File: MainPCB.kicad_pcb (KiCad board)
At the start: 4 copper layers, 105 x 62.4 mm, 57 parts, among them J1 RaspberryPi, J2 Conn_01x05, J3 Screw_Terminal_01x02, J4 Conn_01x02, J5 Conn_01x06, J6 Conn_01x03_Pin, J7 Conn_01x05, J8 Conn_01x12, M1 Motor_DC, M2 Motor_DC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

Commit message: moved more stuff
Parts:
- added J10: Conn_01x02, Connector_PinHeader_2.54mm:PinHeader_1x02_P2.54mm_Vertical, F.Cu at (131.6, 65.5)
- added J9: Conn_01x02, Connector_PinHeader_2.54mm:PinHeader_1x02_P2.54mm_Vertical, F.Cu at (111.8, 120.9)
- moved J2 3.65 mm to (189.5, 93.1)
- moved M1 1.79 mm to (115.1, 82.1)
- moved M4 0.93 mm to (124.5, 74.2)
- moved U5 0.63 mm to (128.3, 76.6)
- moved R1 0.51 mm to (99.6, 93.5)
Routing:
- net 12V: track 228.8 -> 0.00 mm
- net 5V: track 23.1 -> 0.00 mm
- net Net-(J3-Pin_2): track 156.8 -> 159.0 mm

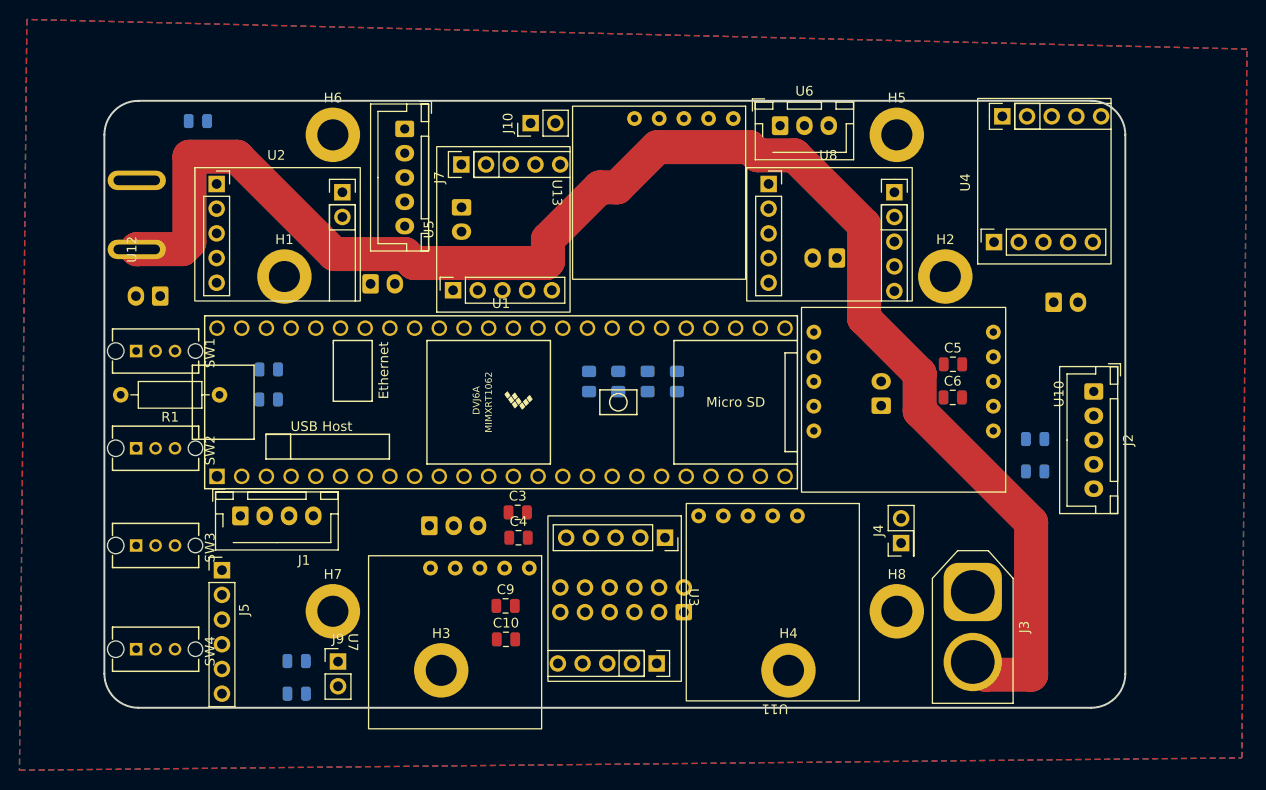
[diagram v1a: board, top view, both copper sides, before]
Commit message: Finished Routing
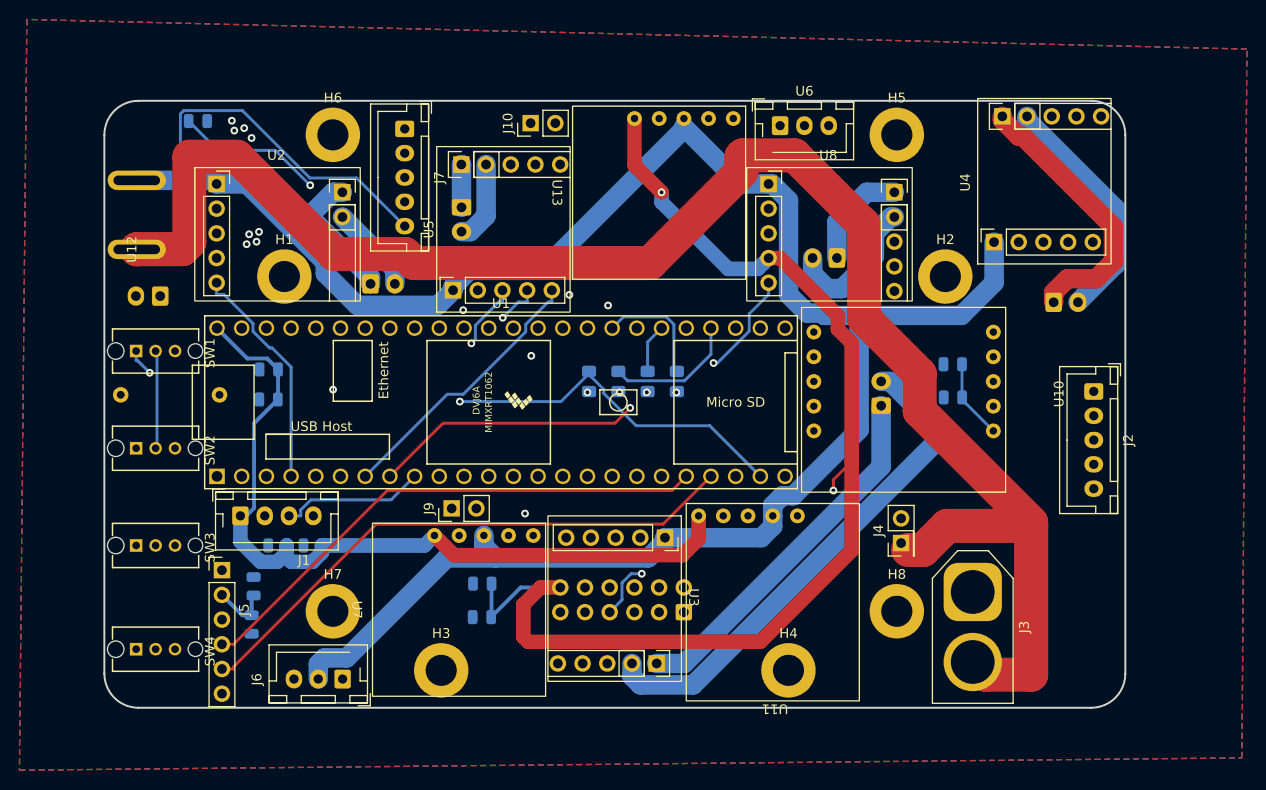
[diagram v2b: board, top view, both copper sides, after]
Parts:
- removed C11, C12: .1uf, Capacitor_SMD:C_0805_2012Metric
- C1: value 10uf -> .1uf
- C10, C3, C4, C5, R1: moved to B.Cu
- C6, C9: value .1uf -> 10uf; moved to B.Cu
- C8: value .1uf -> 10uf
- J6: moved to F.Cu
- moved C3 24.9 mm to (105.5, 109.0), turned to 180 degrees
- moved C4 21.2 mm to (109.2, 109.0), turned to 180 degrees
- moved J9 19.6 mm to (123.4, 105.2), turned to 90 degrees
- moved J6 18.1 mm to (112.2, 122.7), turned to 180 degrees
- moved R1 10.2 mm to (89.4, 93.5), turned to 0 degrees
- moved C8 8.87 mm to (103.1, 113.2), turned to 90 degrees
- moved C7 8.49 mm to (102.9, 117.1), turned to -90 degrees
- moved U7 3.37 mm to (124.2, 115.6)
- moved C10 3.37 mm to (126.6, 116.3), turned to 180 degrees
- moved C9 3.31 mm to (126.6, 112.9), turned to 180 degrees
- turned C5 to 180 degrees
- turned C6 to 180 degrees
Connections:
- J8 pad 9: 5V -> unconnected-(J8-Pin_9-Pad9)
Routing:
- net 3.3V: track 0.00 -> 276.8 mm, vias 0 -> 2
- net 12V: track 0.00 -> 205.7 mm
- net 5V: track 0.00 -> 155.2 mm
- net Net-(J2-Pin_5): track 0.00 -> 116.0 mm
- net PWM3: track 0.00 -> 93.5 mm, vias 0 -> 1
- net DIR3B: track 0.00 -> 86.6 mm
- net SLIDE4: track 0.00 -> 84.6 mm, vias 0 -> 2
- net SLIDE2: track 0.00 -> 84.6 mm
- net SLIDE3: track 0.00 -> 79.2 mm
- net STATE: track 0.00 -> 78.3 mm
- net SLIDE1: track 0.00 -> 74.8 mm, vias 0 -> 3
- net DIR3A: track 0.00 -> 69.0 mm, vias 0 -> 1
- net ECHO: track 0.00 -> 68.3 mm, vias 0 -> 1
- net TX7 -> RX: track 0.00 -> 58.6 mm
- net Kicker: track 0.00 -> 55.3 mm
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
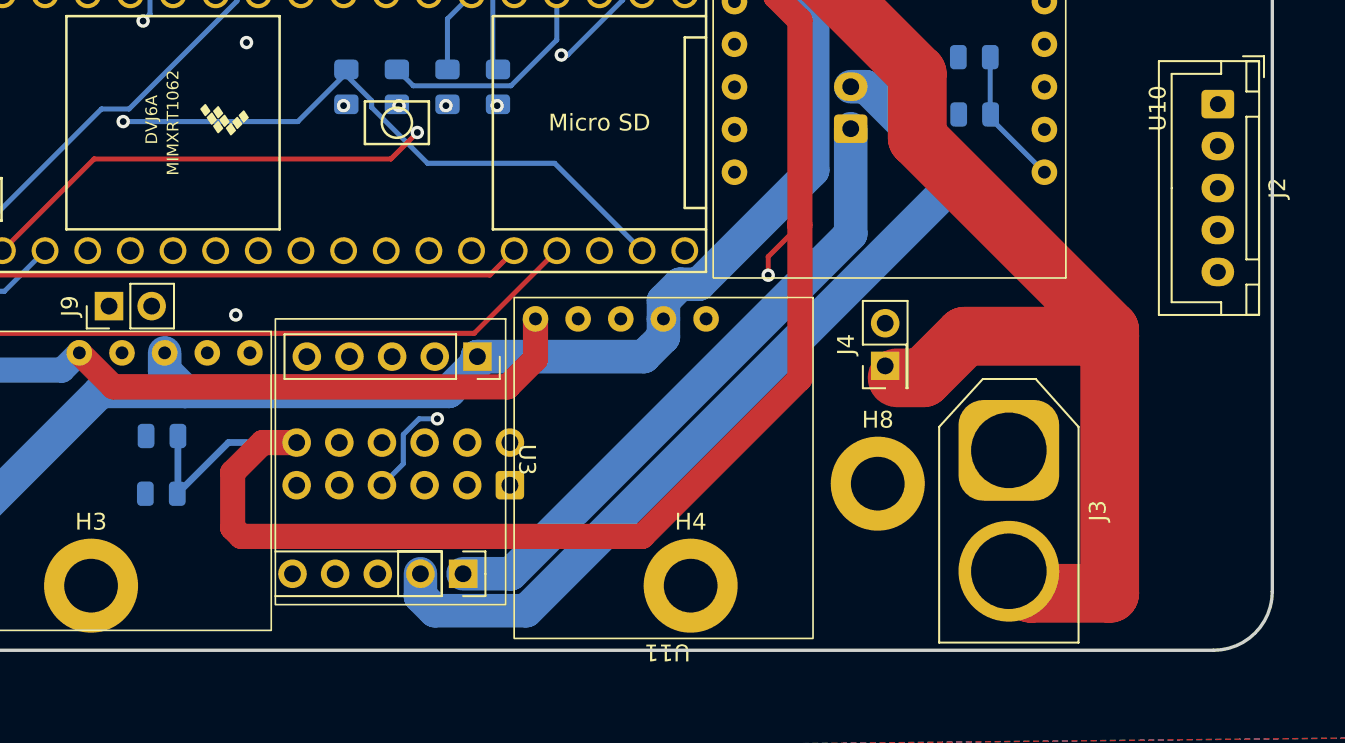
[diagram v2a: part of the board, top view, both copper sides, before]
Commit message: fixed ultrasonic voltages
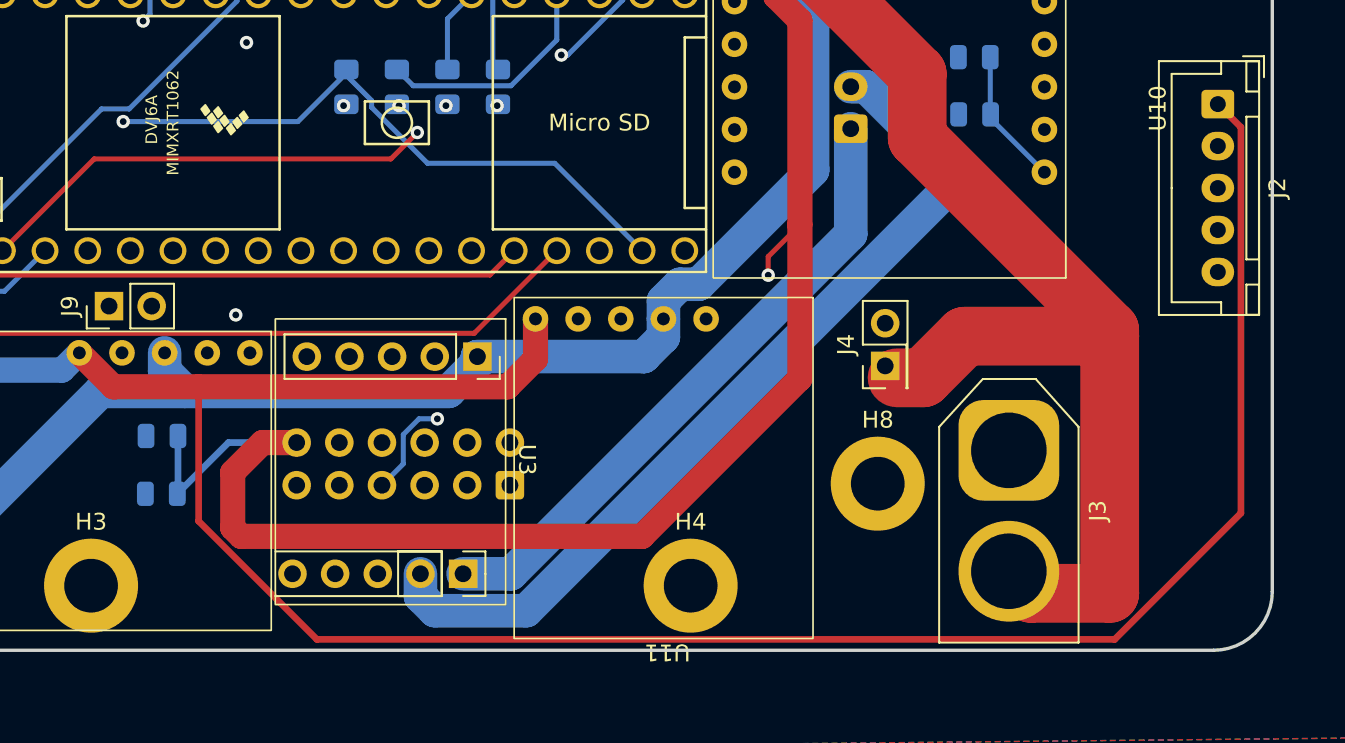
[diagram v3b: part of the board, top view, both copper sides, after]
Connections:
- J2 pad 1: 3.3V -> 5V
- J7 pad 1: 3.3V -> 5V
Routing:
- net 5V: track 155.2 -> 258.1 mm
- net 3.3V: track 276.8 -> 240.0 mm
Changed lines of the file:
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@@
 			(remove_unused_layers no)
 			(net 1 "GND")
-			(pinfunction "OUT-")
+			(pinfunction "IN-")
 			(pintype "input")
 		)
@@
 			(remove_unused_layers no)
 			(roundrect_rratio 0.147059)
-			(net 6 "3.3V")
+			(net 3 "5V")
 			(pinfunction "Pin_1")
 			(pintype "passive")
@@
 			(remove_unused_layers no)
 			(roundrect_rratio 0.147059)
-			(net 6 "3.3V")
+			(net 3 "5V")
 			(pinfunction "Pin_1")
 			(pintype "passive")
@@
 	)
 	(segment
-		(start 121.676 107.94)
-		(end 123.7 109.964)
+		(start 128.778 109.964)
+		(end 147.185 109.964)
 		(width 1.5)
 		(layer "F.Cu")
@@
 	(segment
 		(start 123.7 109.964)
-		(end 147.185 109.964)
+		(end 128.778 109.964)
 		(width 1.5)
 		(layer "F.Cu")
@@
 	)
 	(segment
+		(start 121.676 107.94)
+		(end 123.7 109.964)
+		(width 1.5)
+		(layer "F.Cu")
+		(net 3)
+	)
+	(segment
+		(start 183.341759 125.0068)
+		(end 135.826454 125.0068)
+		(width 0.4)
+		(layer "F.Cu")
+		(net 3)
+	)
+	(segment
+		(start 135.826454 125.0068)
+		(end 128.778 117.958346)
+		(width 0.4)
+		(layer "F.Cu")
+		(net 3)
+	)
+	(segment
+		(start 190.859 117.489559)
+		(end 183.341759 125.0068)
+		(width 0.4)
+		(layer "F.Cu")
+		(net 3)
+	)
+	(segment
+		(start 190.859 94.499)
+		(end 190.859 117.489559)
+		(width 0.4)
+		(layer "F.Cu")
+		(net 3)
+	)
+	(segment
 		(start 148.844 108.306)
 		(end 148.844 105.918)
@@
 	)
 	(segment
-		(start 99.822 114.046)
-		(end 99.822 112.7941)
+		(start 189.484 93.124)
+		(end 190.859 94.499)
 		(width 0.4)
-		(layer "In1.Cu")
+		(layer "F.Cu")
 		(net 3)
 	)
 	(segment
-		(start 117.671 64.817)
-		(end 116.37 66.118)
+		(start 128.778 117.958346)
+		(end 128.778 109.964)
+		(width 0.4)
+		(layer "F.Cu")
+		(net 3)
+	)
+	(segment
+		(start 99.822 114.046)
+		(end 99.822 112.7941)
 		(width 0.4)
 		(layer "In1.Cu")
@@
 	)
 	(segment
+		(start 117.961 65.463)
+		(end 118.618 66.12)
+		(width 0.4)
+		(layer "In1.Cu")
+		(net 3)
+	)
+	(segment
 		(start 123.2081 106.4079)
 		(end 123.444 106.4079)
@@
 	)
 	(segment
+		(start 117.025 65.463)
+		(end 117.961 65.463)
+		(width 0.4)
+		(layer "In1.Cu")
+		(net 3)
+	)
+	(segment
 		(start 131.567 65.532)
 		(end 130.3151 65.532)
@@
 	)
 	(segment
+		(start 117.671 64.817)
+		(end 117.025 65.463)
+		(width 0.4)
+		(layer "In1.Cu")
+		(net 3)
+	)
+	(segment
 		(start 110.744 83.3424)
 		(end 110.744 87.0947)
@@
 	)
 	(segment
+		(start 117.025 65.463)
+		(end 116.37 66.118)
+		(width 0.4)
+		(layer "In1.Cu")
+		(net 3)
+	)
+	(segment
 		(start 116.37 77.7164)
 		(end 110.744 83.3424)
@@
 	)
 	(segment
-		(start 120.4774 64.2606)
-		(end 141.4571 64.2606)
-		(width 0.3)
-		(layer "In2.Cu")
-		(net 6)
-	)
-	(segment
-		(start 118.618 66.12)
-		(end 120.4774 64.2606)
-		(width 0.3)
-		(layer "In2.Cu")
-		(net 6)
-	)
-	(segment
 		(start 119.2373 113.284)
 		(end 134.62 113.284)
@@
 	)
 	(segment
-		(start 189.484 93.124)
-		(end 183.212 93.124)
-		(width 0.3)
-		(layer "In2.Cu")
-		(net 6)
-	)
-	(segment
-		(start 183.212 93.124)
-		(end 179.156 97.18)
-		(width 0.3)
-		(layer "In2.Cu")
-		(net 6)
-	)
-	(segment
 		(start 98.392 120.3961)
 		(end 112.1252 120.3961)
@@
 		(width 0.3)
 		(layer "In2.Cu")
-		(net 6)
-	)
-	(segment
-		(start 141.4571 64.2606)
-		(end 142.25 65.0535)
-		(width 0.3)
-		(layer "In2.Cu")

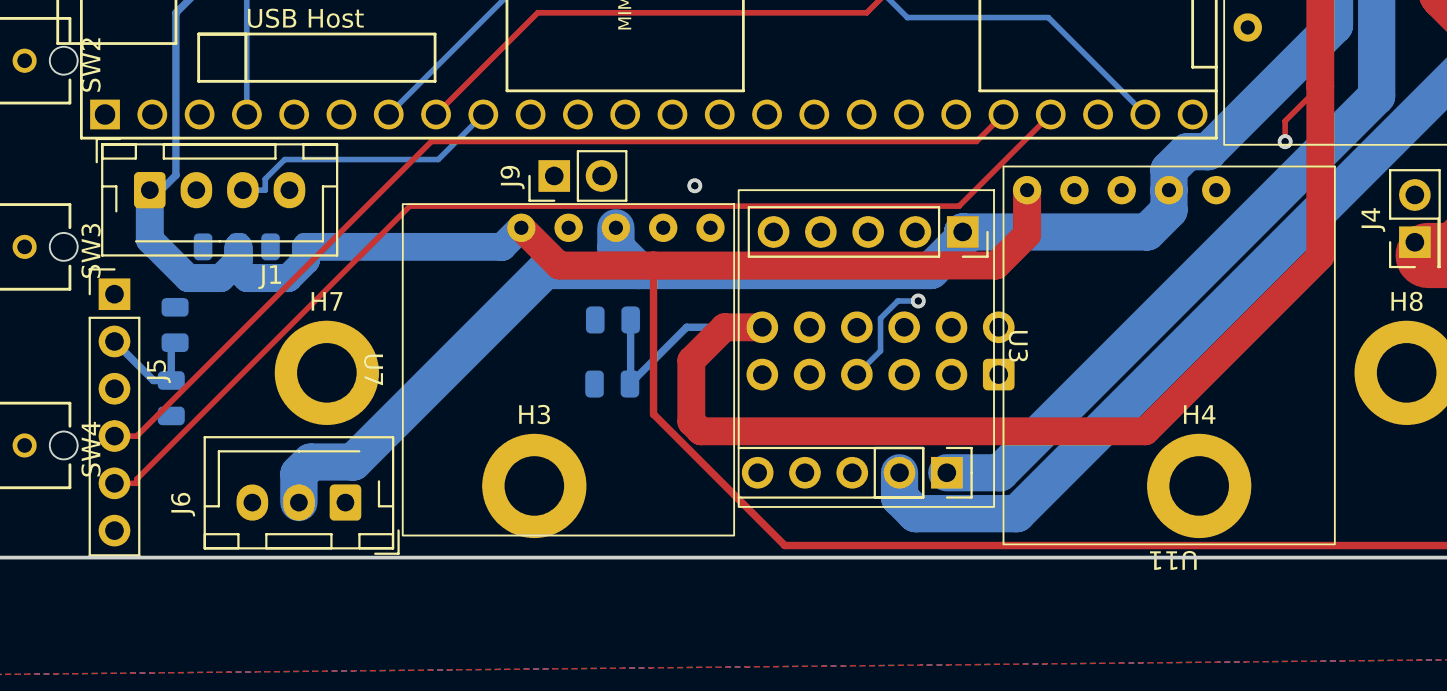
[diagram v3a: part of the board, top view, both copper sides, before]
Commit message: Moved regulators
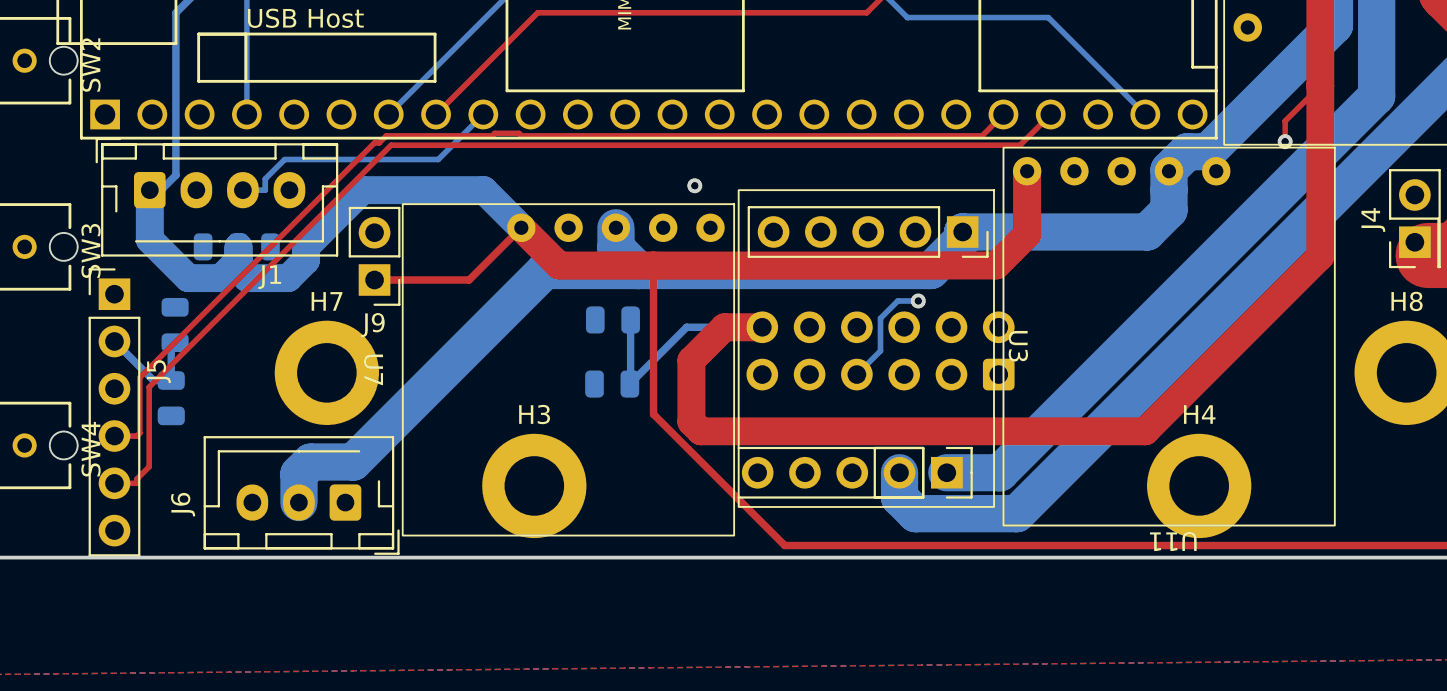
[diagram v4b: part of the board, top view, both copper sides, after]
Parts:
- moved J9 11.2 mm to (113.8, 110.7), turned to 180 degrees
- moved U11 1.02 mm to (165.4, 103.6)
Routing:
- net 5V: track 258.1 -> 266.2 mm
- net TX7 -> RX: track 58.6 -> 61.1 mm
- net RX7 -> TX: track 54.9 -> 56.8 mm
- net CS2: track 52.2 -> 54.1 mm

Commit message: 1:17
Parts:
- moved C8 4.87 mm to (106.9, 116.2)
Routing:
- net 12V: track 205.7 -> 270.3 mm
- net GND: track 16.9 -> 24.8 mm, vias 12 -> 13
- net Net-(M2--): track 52.4 -> 53.8 mm
- net Net-(M2-+): track 37.7 -> 39.2 mm
- net 5V: track 266.2 -> 265.2 mm, vias 0 -> 3
- net TX2->RX: track 20.5 -> 19.6 mm
- net TRIG4: track 31.4 -> 30.7 mm
